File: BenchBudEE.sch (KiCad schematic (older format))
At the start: 0 parts

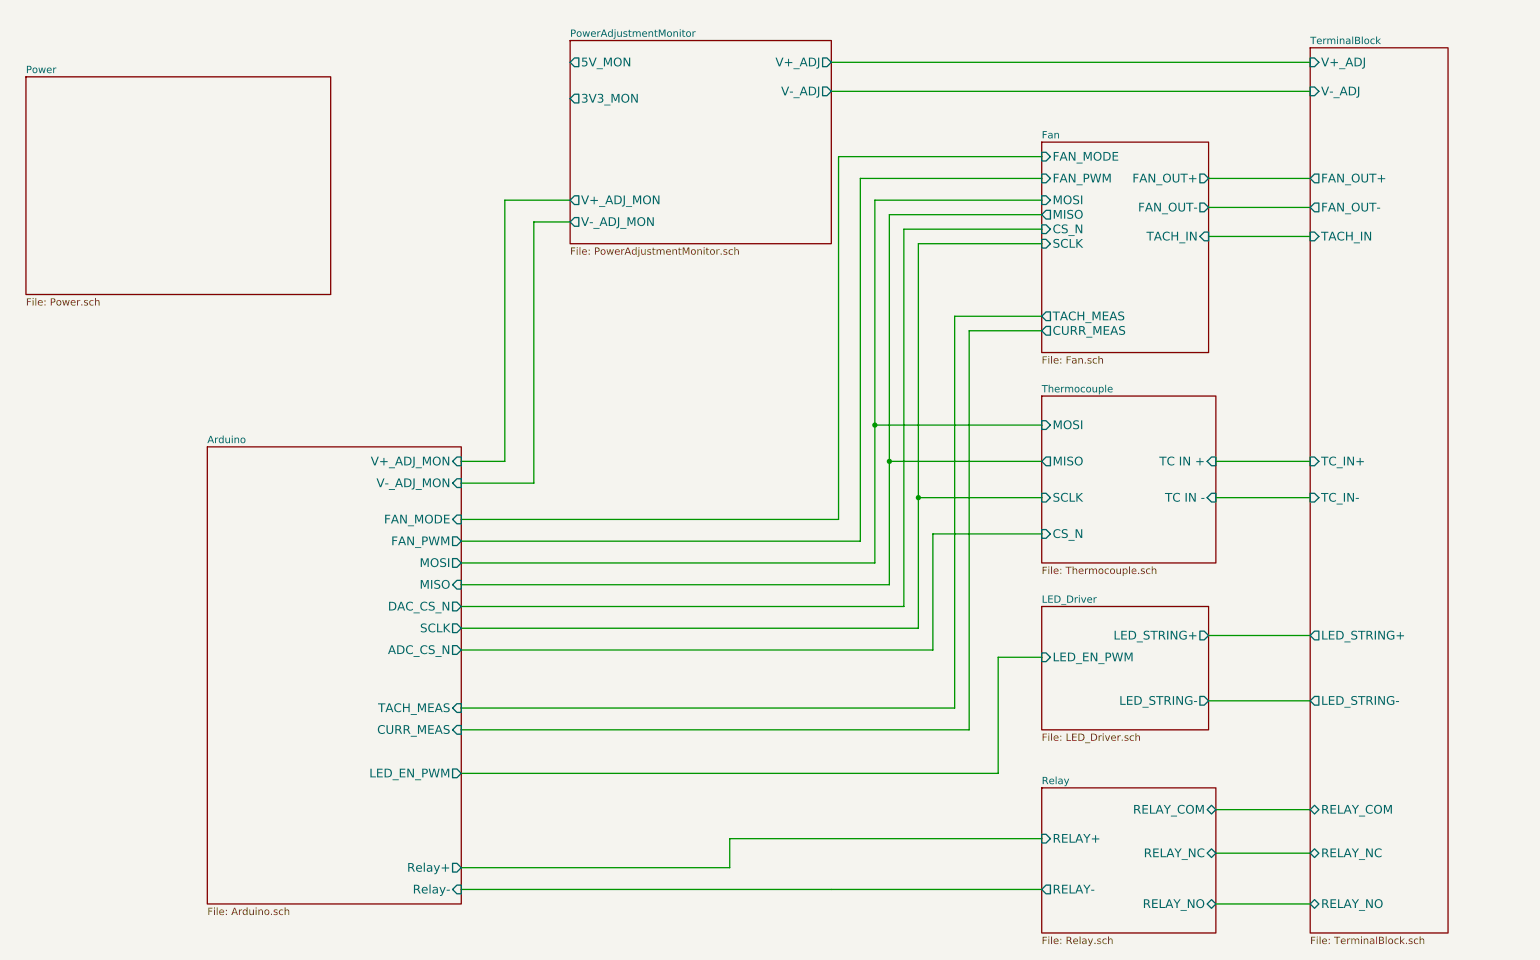
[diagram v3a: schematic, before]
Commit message: Relay module association and placement
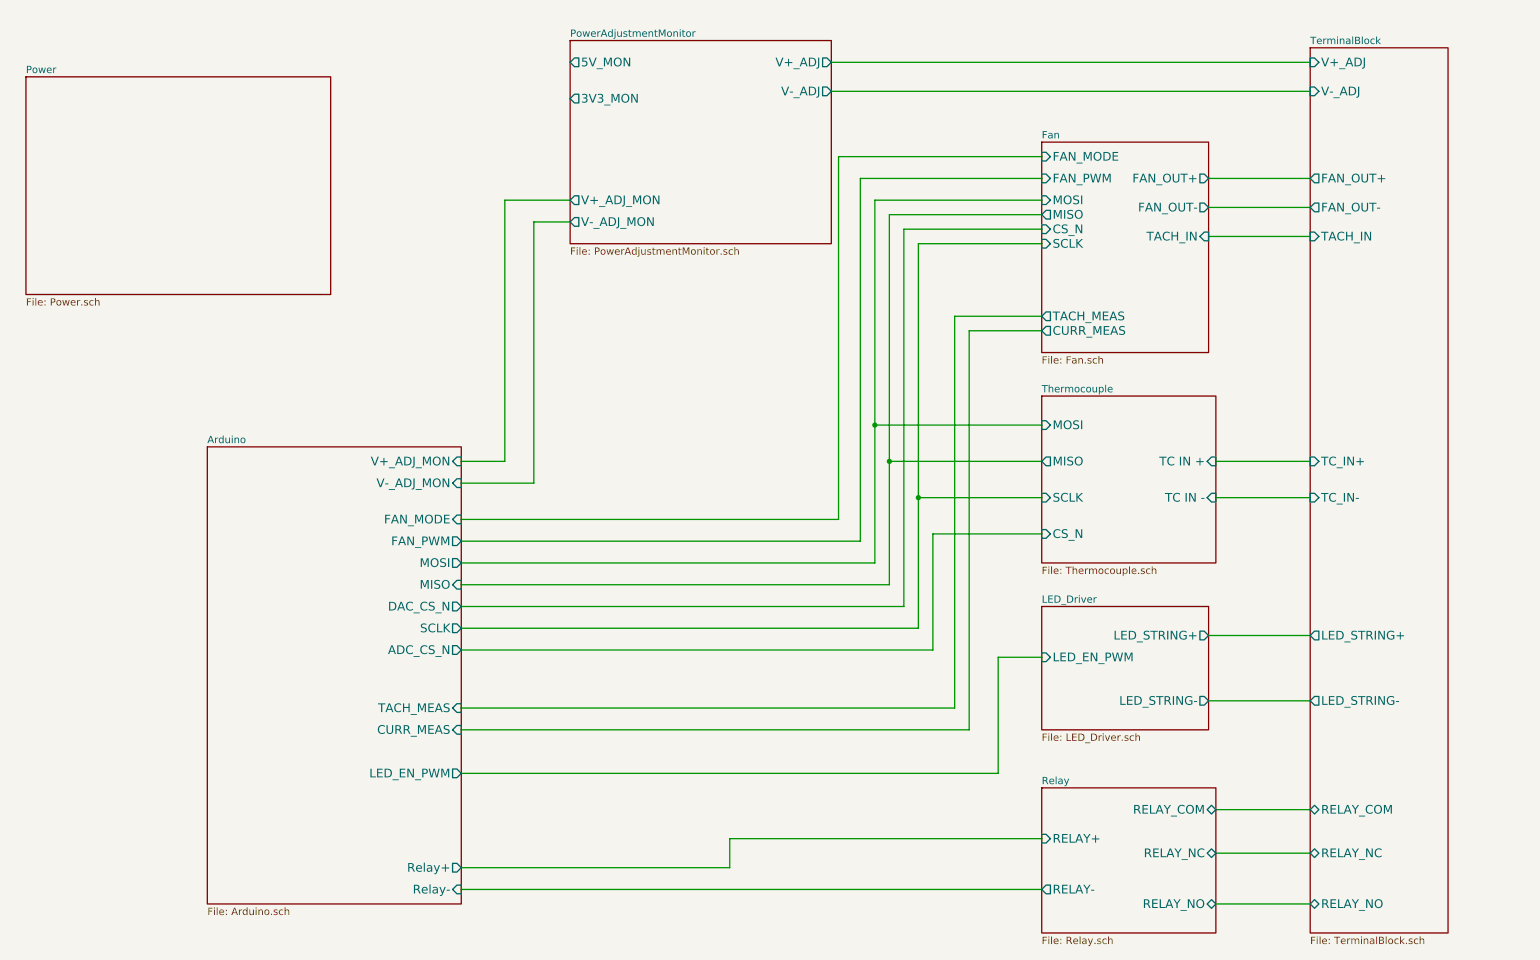
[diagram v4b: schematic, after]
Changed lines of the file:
@@
 Sheet 1 9
 Title ""
-Date "18 feb 2014"
+Date "20 feb 2014"
 Rev ""
 Comp ""
@@
 	7050 4450 4200 4450
 Wire Wire Line
-	7050 1950 7050 3500
-Wire Wire Line
-	7050 3500 7050 4450
+	7050 1950 7050 4450
 Wire Wire Line
 	7050 1950 8200 1950
@@
 	7150 4600 4200 4600
 Wire Wire Line
-	7150 2050 7150 3750
-Wire Wire Line
-	7150 3750 7150 4600
+	7150 2050 7150 4600
 Wire Wire Line
 	7150 2050 8200 2050
@@
 	7350 4900 4200 4900
 Wire Wire Line
-	7350 2250 7350 4000
-Wire Wire Line
-	7350 4000 7350 4900
+	7350 2250 7350 4900
 Wire Wire Line
 	7350 2250 8200 2250
@@
 	6050 6350 8200 6350
 Wire Wire Line
-	4200 6700 6750 6700
-Wire Wire Line
-	6750 6700 6750 6700
-Wire Wire Line
-	6750 6700 8200 6700
+	4200 6700 8200 6700
 Wire Wire Line
 	8200 1650 6800 1650

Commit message: Thermocouple association and placement
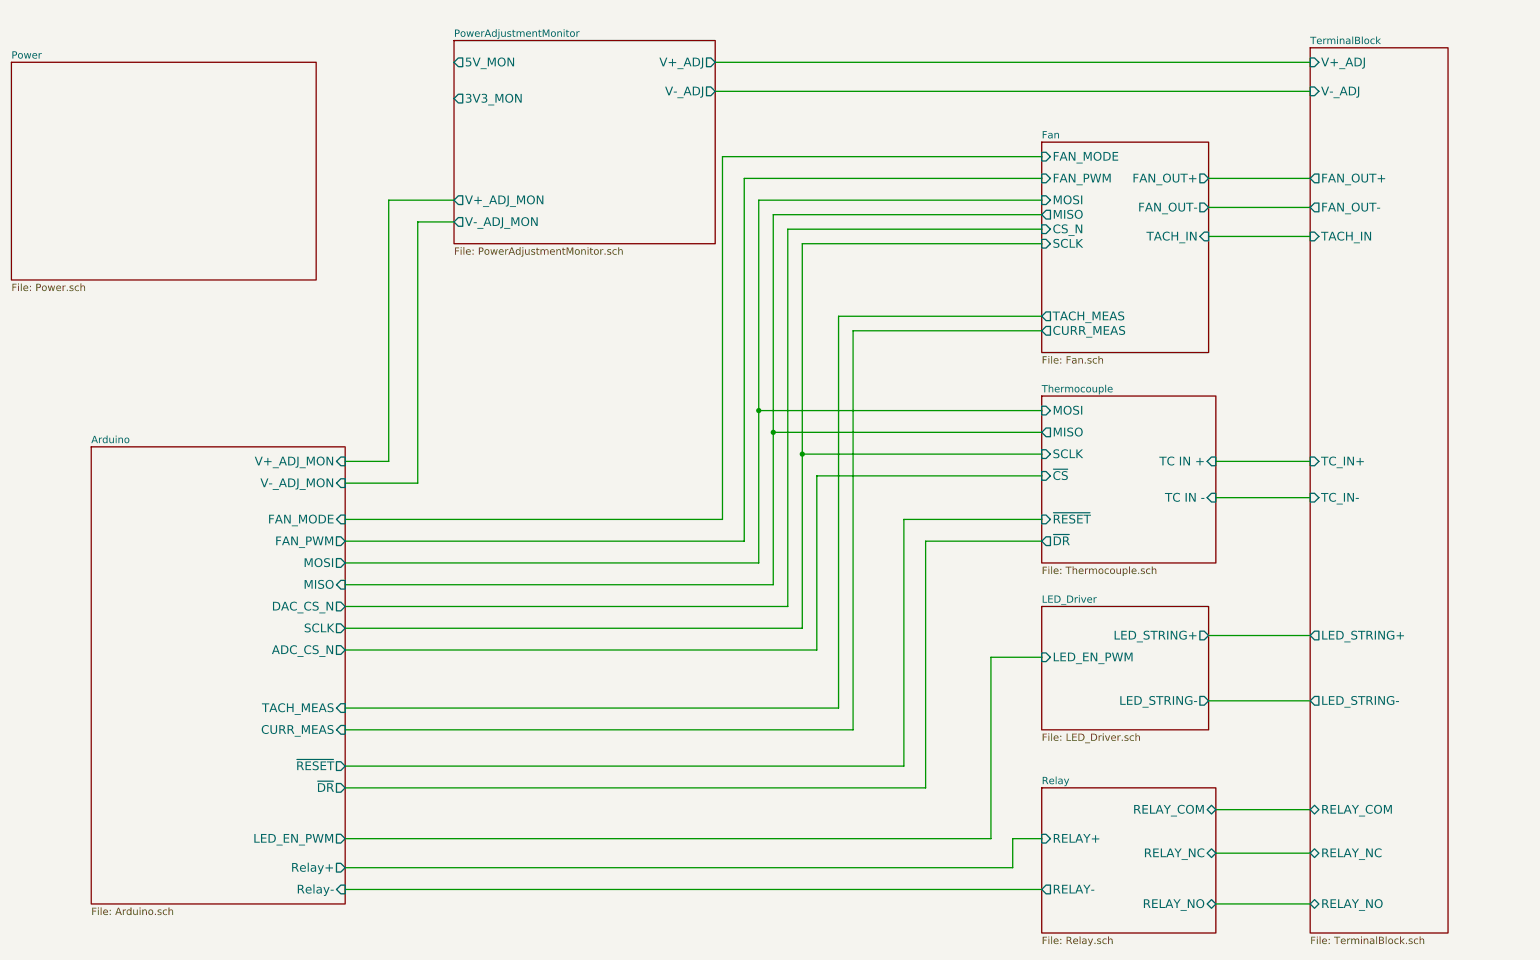
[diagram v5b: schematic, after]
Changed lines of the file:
@@
 Sheet 1 9
 Title ""
-Date "20 feb 2014"
+Date "21 feb 2014"
 Rev ""
 Comp ""
@@
 $EndDescr
 $Sheet
-S 8200 3300 1200 1150
-U 52F2E40C
-F0 "Thermocouple" 50
-F1 "Thermocouple.sch" 50
-F2 "TC IN +" I R 9400 3750 60
-F3 "TC IN -" I R 9400 4000 60
-F4 "MOSI" I L 8200 3500 60
-F5 "MISO" O L 8200 3750 60
-F6 "SCLK" I L 8200 4000 60
-F7 "CS_N" I L 8200 4250 60
-$EndSheet
-$Sheet
-S 1200 1100 2100 1500
+S 1100 1000 2100 1500
 U 52F2E422
 F0 "Power" 50
@@
 $EndSheet
 $Sheet
-S 4950 850  1800 1400
+S 4150 850  1800 1400
 U 52F67DEA
 F0 "PowerAdjustmentMonitor" 50
 F1 "PowerAdjustmentMonitor.sch" 50
-F2 "V+_ADJ" O R 6750 1000 60
-F3 "V-_ADJ" O R 6750 1200 60
-F4 "3V3_MON" O L 4950 1250 60
-F5 "5V_MON" O L 4950 1000 60
-F6 "V+_ADJ_MON" O L 4950 1950 60
-F7 "V-_ADJ_MON" O L 4950 2100 60
+F2 "V+_ADJ" O R 5950 1000 60
+F3 "V-_ADJ" O R 5950 1200 60
+F4 "3V3_MON" O L 4150 1250 60
+F5 "5V_MON" O L 4150 1000 60
+F6 "V+_ADJ_MON" O L 4150 1950 60
+F7 "V-_ADJ_MON" O L 4150 2100 60
 $EndSheet
 $Sheet
@@
 	9350 1800 10050 1800
 Wire Wire Line
-	6750 1000 10050 1000
-Wire Wire Line
-	10050 1200 6750 1200
-Wire Wire Line
-	4200 3750 4500 3750
-Wire Wire Line
-	4500 3750 4500 1950
-Wire Wire Line
-	4500 1950 4950 1950
-Wire Wire Line
-	4200 3900 4700 3900
-Wire Wire Line
-	4700 3900 4700 2100
-Wire Wire Line
-	4700 2100 4950 2100
-Wire Wire Line
-	4200 4300 6950 4300
-Wire Wire Line
-	6950 4300 6950 1800
-Wire Wire Line
-	6950 1800 8200 1800
-Wire Wire Line
-	7050 4450 4200 4450
-Wire Wire Line
-	7050 1950 7050 4450
-Wire Wire Line
-	7050 1950 8200 1950
-Wire Wire Line
-	7150 4600 4200 4600
-Wire Wire Line
-	7150 2050 7150 4600
-Wire Wire Line
-	7150 2050 8200 2050
-Wire Wire Line
-	4200 4750 7250 4750
-Wire Wire Line
-	7250 4750 7250 2150
-Wire Wire Line
-	7250 2150 8200 2150
-Wire Wire Line
-	7350 4900 4200 4900
-Wire Wire Line
-	7350 2250 7350 4900
-Wire Wire Line
-	7350 2250 8200 2250
+	5950 1000 10050 1000
+Wire Wire Line
+	10050 1200 5950 1200
+Wire Wire Line
+	3400 3750 3700 3750
+Wire Wire Line
+	3700 3750 3700 1950
+Wire Wire Line
+	3700 1950 4150 1950
+Wire Wire Line
+	3400 3900 3900 3900
+Wire Wire Line
+	3900 3900 3900 2100
+Wire Wire Line
+	3900 2100 4150 2100
+Wire Wire Line
+	3400 4300 6150 4300
+Wire Wire Line
+	6150 4300 6150 1800
+Wire Wire Line
+	6150 1800 8200 1800
+Wire Wire Line
+	6250 4450 3400 4450
+Wire Wire Line
+	6250 1950 6250 4450
+Wire Wire Line
+	6250 1950 8200 1950
+Wire Wire Line
+	6350 4600 3400 4600
+Wire Wire Line
+	6350 2050 6350 4600
+Wire Wire Line
+	6350 2050 8200 2050
+Wire Wire Line
+	3400 4750 6450 4750
+Wire Wire Line
+	6450 4750 6450 2150
+Wire Wire Line
+	6450 2150 8200 2150
+Wire Wire Line
+	6550 4900 3400 4900
+Wire Wire Line
+	6550 2250 6550 4900
+Wire Wire Line
+	6550 2250 8200 2250
 Wire Wire Line
 	9400 3750 10050 3750
@@
 	10050 5400 9350 5400
 Wire Wire Line
-	8200 3500 7050 3500
-Connection ~ 7050 3500
-Wire Wire Line
-	8200 3750 7150 3750
-Connection ~ 7150 3750
-Wire Wire Line
-	8200 4000 7350 4000
-Connection ~ 7350 4000
-Wire Wire Line
-	4200 5050 7450 5050
-Wire Wire Line
-	7450 5050 7450 4250
-Wire Wire Line
-	7450 4250 8200 4250
-$Sheet
-S 2450 3650 1750 3150
+	8200 3400 6250 3400
+Connection ~ 6250 3400
+Wire Wire Line
+	8200 3550 6350 3550
+Connection ~ 6350 3550
+Wire Wire Line
+	8200 3700 6550 3700
+Connection ~ 6550 3700
+Wire Wire Line
+	3400 5050 6650 5050
+Wire Wire Line
+	6650 5050 6650 3850
+Wire Wire Line
+	6650 3850 8200 3850
+$Sheet
+S 1650 3650 1750 3150
 U 52F2E3BD
 F0 "Arduino" 50
 F1 "Arduino.sch" 50
-F2 "Relay+" O R 4200 6550 60
-F3 "Relay-" I R 4200 6700 60
-F4 "V+_ADJ_MON" I R 4200 3750 60
-F5 "V-_ADJ_MON" I R 4200 3900 60
-F6 "MOSI" O R 4200 4450 60
-F7 "MISO" I R 4200 4600 60
-F8 "SCLK" O R 4200 4900 60
-F9 "TACH_MEAS" I R 4200 5450 60
-F10 "CURR_MEAS" I R 4200 5600 60
-F11 "LED_EN_PWM" O R 4200 5900 60
-F12 "DAC_CS_N" O R 4200 4750 60
-F13 "ADC_CS_N" O R 4200 5050 60
-F14 "FAN_PWM" O R 4200 4300 60
-F15 "FAN_MODE" I R 4200 4150 60
-$EndSheet
-Wire Wire Line
-	4200 5450 7600 5450
-Wire Wire Line
-	7600 5450 7600 2750
-Wire Wire Line
-	7600 2750 8200 2750
-Wire Wire Line
-	8200 2850 7700 2850
-Wire Wire Line
-	7700 2850 7700 5600
-Wire Wire Line
-	7700 5600 4200 5600
-Wire Wire Line
-	4200 5900 7900 5900
-Wire Wire Line
-	7900 5900 7900 5100
-Wire Wire Line
-	7900 5100 8200 5100
-Wire Wire Line
-	4200 6550 6050 6550
-Wire Wire Line
-	6050 6550 6050 6350
-Wire Wire Line
-	6050 6350 8200 6350
-Wire Wire Line
-	4200 6700 8200 6700
-Wire Wire Line
-	8200 1650 6800 1650
-Wire Wire Line
-	6800 1650 6800 4150
-Wire Wire Line
-	6800 4150 4200 4150
+F2 "Relay+" O R 3400 6550 60
+F3 "Relay-" I R 3400 6700 60
+F4 "V+_ADJ_MON" I R 3400 3750 60
+F5 "V-_ADJ_MON" I R 3400 3900 60
+F6 "MOSI" O R 3400 4450 60
+F7 "MISO" I R 3400 4600 60
+F8 "SCLK" O R 3400 4900 60
+F9 "TACH_MEAS" I R 3400 5450 60
+F10 "CURR_MEAS" I R 3400 5600 60
+F11 "LED_EN_PWM" O R 3400 6350 60
+F12 "DAC_CS_N" O R 3400 4750 60
+F13 "ADC_CS_N" O R 3400 5050 60
+F14 "FAN_PWM" O R 3400 4300 60
+F15 "FAN_MODE" I R 3400 4150 60
+F16 "~RESET" O R 3400 5850 60
+F17 "~DR" O R 3400 6000 60
+$EndSheet
+Wire Wire Line
+	3400 5450 6800 5450
+Wire Wire Line
+	6800 5450 6800 2750
+Wire Wire Line
+	6800 2750 8200 2750
+Wire Wire Line
+	8200 2850 6900 2850
+Wire Wire Line
+	6900 2850 6900 5600
+Wire Wire Line
+	6900 5600 3400 5600
+Wire Wire Line
+	3400 6350 7850 6350
+Wire Wire Line
+	7850 6350 7850 5100
+Wire Wire Line
+	7850 5100 8200 5100
+Wire Wire Line
+	3400 6550 8000 6550
+Wire Wire Line
+	8000 6550 8000 6350
+Wire Wire Line
+	8000 6350 8200 6350
+Wire Wire Line
+	3400 6700 8200 6700
+Wire Wire Line
+	8200 1650 6000 1650
+Wire Wire Line
+	6000 1650 6000 4150
+Wire Wire Line
+	6000 4150 3400 4150
 $Sheet
 S 8200 6000 1200 1000
@@
 F6 "RELAY-" O L 8200 6700 60
 $EndSheet
+$Sheet
+S 8200 3300 1200 1150
+U 52F2E40C
+F0 "Thermocouple" 50
+F1 "Thermocouple.sch" 50
+F2 "TC IN +" I R 9400 3750 60
+F3 "TC IN -" I R 9400 4000 60
+F4 "MOSI" I L 8200 3400 60
+F5 "MISO" O L 8200 3550 60
+F6 "SCLK" I L 8200 3700 60
+F8 "~CS" I L 8200 3850 60
+F9 "~DR" O L 8200 4300 60
+F10 "~RESET" I L 8200 4150 60
+$EndSheet
+Wire Wire Line
+	3400 5850 7250 5850
+Wire Wire Line
+	7250 5850 7250 4150
+Wire Wire Line
+	7250 4150 8200 4150
+Wire Wire Line
+	3400 6000 7400 6000
+Wire Wire Line
+	7400 6000 7400 4300
+Wire Wire Line
+	7400 4300 8200 4300
 $EndSCHEMATC
